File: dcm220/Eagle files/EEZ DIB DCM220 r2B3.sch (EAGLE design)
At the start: 228 parts, among them IC1 Si8662AB-B-IS1, IC10 LT3763EFE#PBF, IC11 MC33274ADR2G, IC12 LT3763EFE#PBF, IC2 TPS54060DGQ, IC3 Si8641AB-B-IS1, IC4 M24C32-WMN6P, IC5 LP2985-33DBVR, IC6 TPD4E001DRLR, IC7 MAX5715BAUD+, IC8 STM32F373C8T6, IC9 MC33272ADR2G, J1 4907, J2 571-0500, J3 571-0100, J4 571-0500, J5 571-0100, Q1 IRFR7546TRPBF, Q2 IRFR7546TRPBF, Q3 2N7002, Q4 BSS84, Q5 IRFR7546TRPBF, Q6 IRFR7546TRPBF, Q7 2N7002, Q8 BSS84, X1 172648-0102, X2 77317-104-28LF, X3 22-23-2061, X4 DS1024-2*5R0, Y1 LF XTAL026392

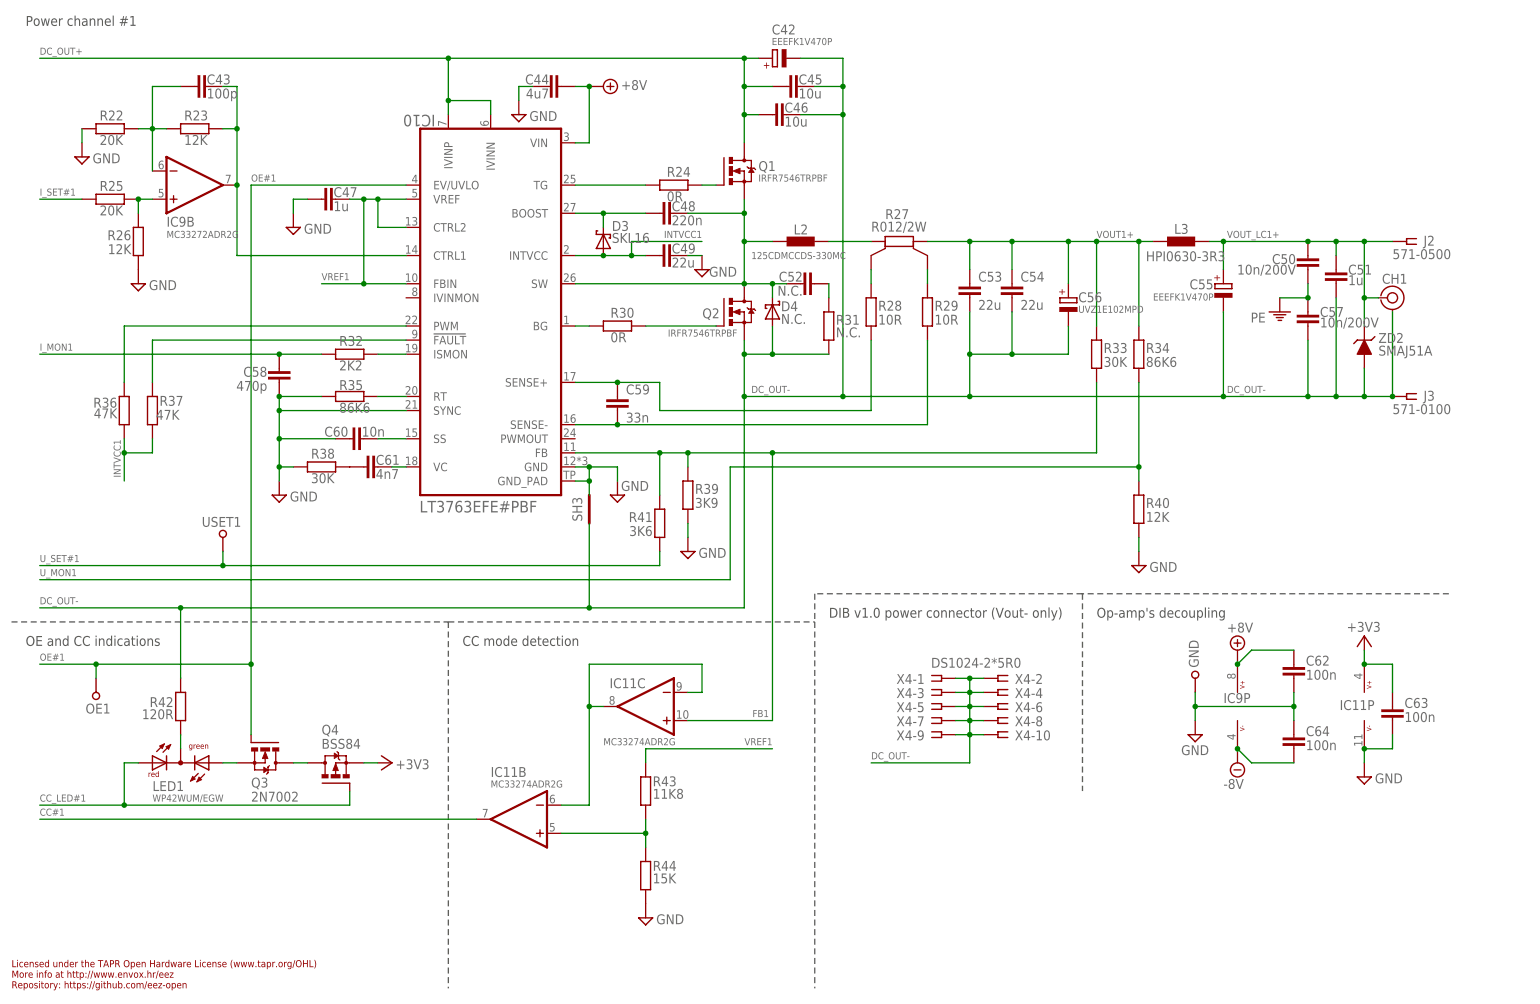
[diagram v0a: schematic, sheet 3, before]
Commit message: #48, replaced DAC with PWM
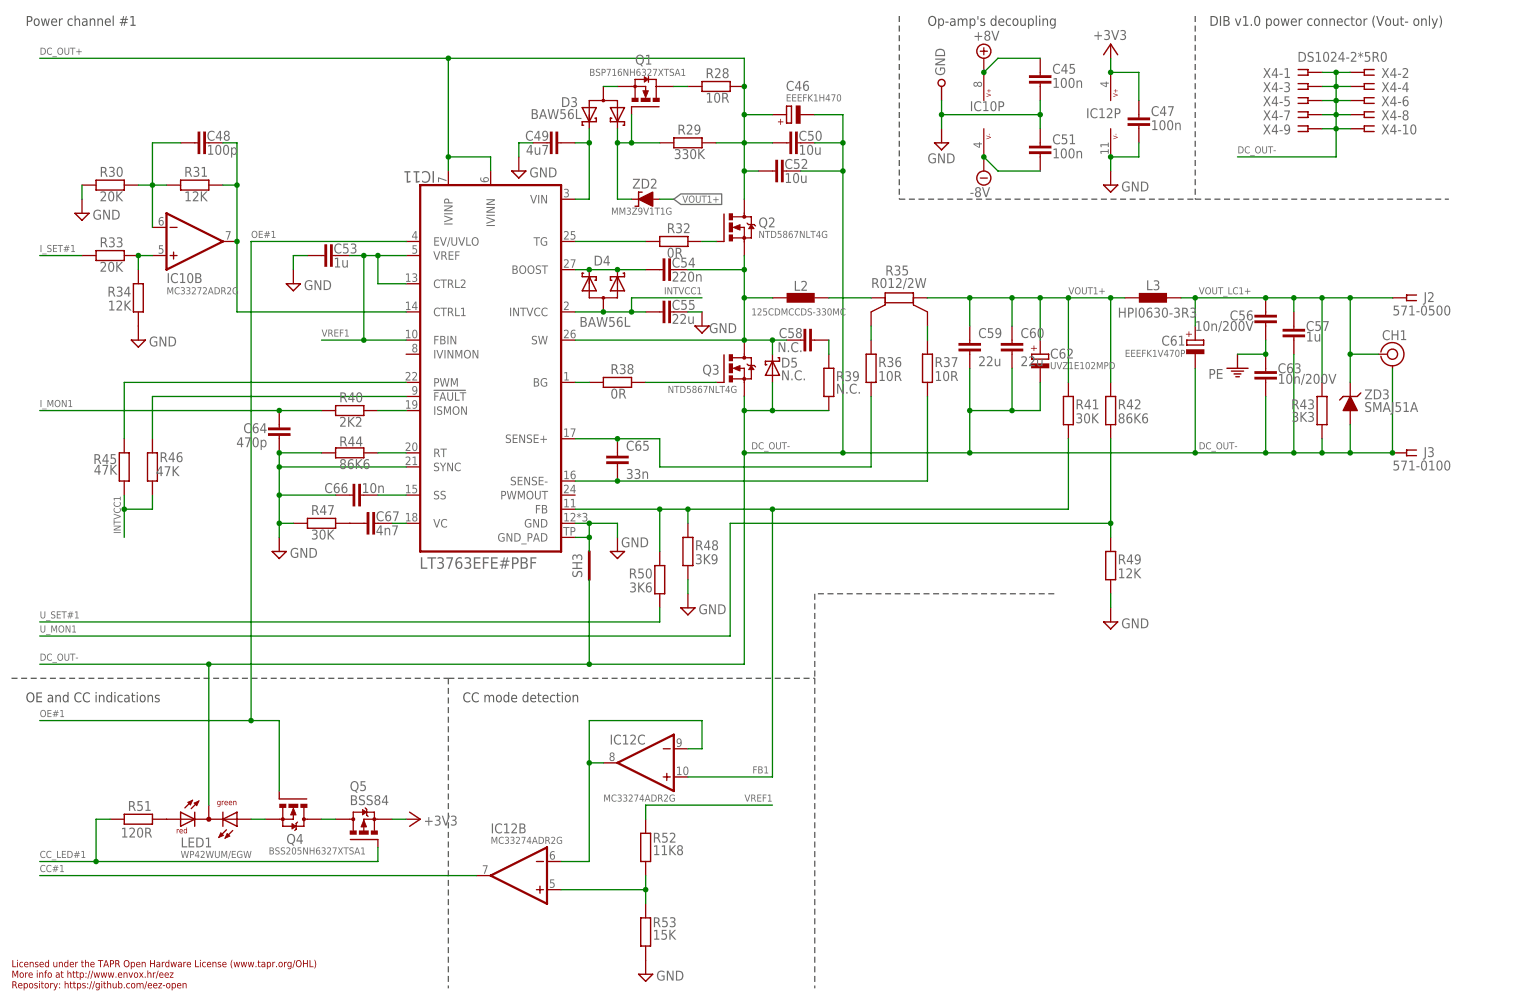
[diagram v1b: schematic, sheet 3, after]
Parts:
- removed ISET1, OE1, USET1: (no value), EEZ_connectors:TEST-PIN_0.9MM
- removed JP4: JP2-CUT, EEZ_Lib1:JP2-CUT
- removed JP5: JP2-NOCUT, EEZ_Lib1:JP2-NOCUT
- added C85: 33n, rcl:C-EUC0805
- added C86: 10n, rcl:C-EUC0805
- added C87: 4n7, rcl:C-EUC0805
- added D7: BAW56L, EEZ_Lib1:BAW56L
- added D8: N.C., EEZ_Lib1:SCHOTTKYSMA_DO-214AC
- added IC13: LT3763EFE#PBF, EEZ_Lib1:LT3763EFE#PBF
- added Q10: BSS84, EEZ_Lib1:IRLML2246TRPBF
- added Q9: BSS205NH6327XTSA1, EEZ_Lib1:2N7002
- added R68, R70: 86K6, rcl:R-EU_R0805
- added R69: 3K3, rcl:R-EU_R0805
- added R71, R72: 47K, rcl:R-EU_R0805
- added R73: 30K, rcl:R-EU_R0805
- added R74: 3K9, rcl:R-EU_R0805
- added R75: 12K, rcl:R-EU_R0805
- added R76: 3K6, rcl:R-EU_R0805
- added R77: 120R, rcl:R-EU_R0805
- added R78: 11K8, rcl:R-EU_R0805
- added R79: 15K, rcl:R-EU_R0805
- added ZD4: MM3Z9V1T1G, EEZ_Lib1:ZENER-DIODESOD323
- added ZD5: SMAJ51A, EEZ_Lib1:P6SMB68A
- C1, C2, C3: value 4n7/100V -> 10n/200V
- C15: value 100n -> 10n; device rcl:C-EUC0603 -> rcl:C-EUC0805
- C25: value 100n -> N.C.
- C26, C27: value 4u7 -> 100n; device rcl:C-EUC1206 -> rcl:C-EUC0603
- C29: value 100n -> 4u7; device rcl:C-EUC0603 -> rcl:C-EUC1206
- C30, C31: value 18p -> 100n
- C32: value 100n -> 4p7
- C33: value 10n -> 4p7; device rcl:C-EUC0805 -> rcl:C-EUC0603
- C35: value 1u -> 10n
- C36: value 100p -> 1n
- C38: value 3n3 -> 1u
- C39, C41: value 3n3 -> 4n7
- C40: value 3n3 -> 100n; device rcl:C-EUC0805 -> rcl:C-EUC0603
- C42: value EEEFK1V470P -> 4n7; device EEZ_Lib1:ECAPSMD8.3MM/HA0 -> rcl:C-EUC0805
- C43: value 100p -> 4n7
- C44, C67: value 4u7 -> 4n7; device rcl:C-EUC1206 -> rcl:C-EUC0805
- C45: value 10u -> 100n; device rcl:C-EUC1210 -> rcl:C-EUC0603
- C46, C68: value 10u -> EEEFK1H470; device rcl:C-EUC1210 -> EEZ_Lib1:ECAPSMD8.3MM/HA0
- C47, C51: value 1u -> 100n; device rcl:C-EUC0805 -> rcl:C-EUC0603
- C48: value 220n -> 100p
- C49: value 22u -> 4u7; device rcl:C-EUC1210 -> rcl:C-EUC1206
- C50: value 10n/200V -> 10u; device rcl:C-EUC1206 -> rcl:C-EUC1210
- C52: value N.C. -> 10u; device rcl:C-EUC0805 -> rcl:C-EUC1210
- C53, C77: value 22u -> 1u; device rcl:C-EUC1210 -> rcl:C-EUC0805
- C54: value 22u -> 220n; device rcl:C-EUC1210 -> rcl:C-EUC0805
- C55: value EEEFK1V470P -> 22u; device EEZ_Lib1:ECAPSMD8.3MM/HA0 -> rcl:C-EUC1210
- C56: value UVZ1E102MPD -> 10n/200V; device EEZ_Lib1:ECAP5G_10.5MM -> rcl:C-EUC1206
- C57, C73: value 10n/200V -> 1u; device rcl:C-EUC1206 -> rcl:C-EUC0805
- C58: value 470p -> N.C.
- C59: value 33n -> 22u; device rcl:C-EUC0805 -> rcl:C-EUC1210
- C60: value 10n -> 22u; device rcl:C-EUC0805 -> rcl:C-EUC1210
- C61: value 4n7 -> EEEFK1V470P; device rcl:C-EUC0805 -> EEZ_Lib1:ECAPPANASONIC_H
- C62: value 100n -> UVZ1E102MPD; device rcl:C-EUC0603 -> EEZ_Lib1:ECAP5G_10.5MM
- C63: value 100n -> 10n/200V; device rcl:C-EUC0603 -> rcl:C-EUC1206
- C64: value 100n -> 470p; device rcl:C-EUC0603 -> rcl:C-EUC0805
- C65: value EEEFK1V470P -> 33n; device EEZ_Lib1:ECAPSMD8.3MM/HA0 -> rcl:C-EUC0805
- C66: value 100p -> 10n
- C69: value 10u -> 100p; device rcl:C-EUC1210 -> rcl:C-EUC0805
- C70: value 1u -> 4u7; device rcl:C-EUC0805 -> rcl:C-EUC1206
- C71: value 220n -> 10u; device rcl:C-EUC0805 -> rcl:C-EUC1210
- C72: value 22u -> 10u
- C74: value 1u -> 220n
- C75: value N.C. -> 22u; device rcl:C-EUC0805 -> rcl:C-EUC1210
- C76: value 22u -> 10n/200V; device rcl:C-EUC1210 -> rcl:C-EUC1206
- C78: value EEEFK1V470P -> N.C.; device EEZ_Lib1:ECAPSMD8.3MM/HA0 -> rcl:C-EUC0805
- C79: value UVZ1E102MPD -> 22u; device EEZ_Lib1:ECAP5G_10.5MM -> rcl:C-EUC1210
- C80: value 10n/200V -> 22u; device rcl:C-EUC1206 -> rcl:C-EUC1210
- C81: value 470p -> EEEFK1V470P; device rcl:C-EUC0805 -> EEZ_Lib1:ECAPPANASONIC_H
- C82: value 33n -> UVZ1E102MPD; device rcl:C-EUC0805 -> EEZ_Lib1:ECAP5G_10.5MM
- C83: value 10n -> 10n/200V; device rcl:C-EUC0805 -> rcl:C-EUC1206
- C84: value 4n7 -> 470p
- D3: value SKL16 -> BAW56L; device EEZ_Lib1:SCHOTTKYSOD123 -> EEZ_Lib1:BAW56L
- D4, D6: value N.C. -> BAW56L; device EEZ_Lib1:SCHOTTKYSMA_DO-214AC -> EEZ_Lib1:BAW56L
- D5: value SKL16 -> N.C.; device EEZ_Lib1:SCHOTTKYSOD123 -> EEZ_Lib1:SCHOTTKYSMA_DO-214AC
- IC10: value LT3763EFE#PBF -> MC33272ADR2G; device EEZ_Lib1:LT3763EFE#PBF -> EEZ_Lib1:TL072SOIC8
- IC11: value MC33274ADR2G -> LT3763EFE#PBF; device EEZ_Lib1:TL074SOIC14 -> EEZ_Lib1:LT3763EFE#PBF
- IC12: value LT3763EFE#PBF -> MC33274ADR2G; device EEZ_Lib1:LT3763EFE#PBF -> EEZ_Lib1:TL074SOIC14
- IC6: value TPD4E001DRLR -> 74HC2G04GW,125; device EEZ_Lib1:TPD4E001-DRL -> EEZ_Lib1:74HC2G04
- IC7: value MAX5715BAUD+ -> N.C.; device EEZ_Lib1:MAX5715BAUD+ -> EEZ_Lib1:TPD4E001-DRL
- IC9: value MC33272ADR2G -> TL431B; device EEZ_Lib1:TL072SOIC8 -> EEZ_Lib1:TL431
- JP2: value JP2-NOCUT -> JP2-CUT; device EEZ_Lib1:JP2-NOCUT -> EEZ_Lib1:JP2-CUT
- Q1, Q6: value IRFR7546TRPBF -> BSP716NH6327XTSA1; device EEZ_Lib1:N-MOSFETDPAK -> transistor-power:N-HEXFET-2D_SOT232-IRLL014N
- Q2: value IRFR7546TRPBF -> NTD5867NLT4G
- Q3, Q7: value 2N7002 -> NTD5867NLT4G; device EEZ_Lib1:2N7002 -> EEZ_Lib1:N-MOSFETDPAK
- Q4: value BSS84 -> BSS205NH6327XTSA1; device EEZ_Lib1:IRLML2246TRPBF -> EEZ_Lib1:2N7002
- Q5: value IRFR7546TRPBF -> BSS84; device EEZ_Lib1:N-MOSFETDPAK -> EEZ_Lib1:IRLML2246TRPBF
- Q8: value BSS84 -> NTD5867NLT4G; device EEZ_Lib1:IRLML2246TRPBF -> EEZ_Lib1:N-MOSFETDPAK
- R1: value 4K7/2W -> N.C.
- R16, R17: value 3K3 -> 10K
- R18, R20: value 1K -> 10K
- R19: value 1K -> N.C.
- R21: value 1K -> 3K3
- R22: value 20K -> 3K3
- R23: value 12K -> 120R
- R24: value 0R -> 2K2
- R25: value 20K -> 2K2
- R26, R40: value 12K -> 2K2
- R27: value R012/2W -> 2K2; device EEZ_Lib1:R-EU_4WIRE2512 -> rcl:R-EU_R0805
- R29: value 10R -> 330K
- R30: value 0R -> 20K
- R31: value N.C. -> 12K; device rcl:R-EU_R1206 -> rcl:R-EU_R0805
- R32: value 2K2 -> 0R
- R33, R56: value 30K -> 20K
- R34, R57: value 86K6 -> 12K
- R35: value 86K6 -> R012/2W; device rcl:R-EU_R0805 -> EEZ_Lib1:R-EU_4WIRE2512
- R36, R37: value 47K -> 10R
- R38: value 30K -> 0R
- R39: value 3K9 -> N.C.; device rcl:R-EU_R0805 -> rcl:R-EU_R1206
- R41: value 3K6 -> 30K
- R42: value 120R -> 86K6
- R43: value 11K8 -> 3K3
- R44: value 15K -> 86K6
- R45: value 20K -> 47K
- R46: value 12K -> 47K
- R47: value 0R -> 30K
- R48: value 20K -> 3K9
- R50: value R012/2W -> 3K6; device EEZ_Lib1:R-EU_4WIRE2512 -> rcl:R-EU_R0805
- R51: value 10R -> 120R
- R52: value 10R -> 11K8
- R53: value 0R -> 15K
- R54: value N.C. -> 10R; device rcl:R-EU_R1206 -> rcl:R-EU_R0805
- R55: value 2K2 -> 330K
- R58: value 86K6 -> 0R
- R59: value 47K -> 20K
- R60: value 47K -> 12K
- R61: value 30K -> R012/2W; device rcl:R-EU_R0805 -> EEZ_Lib1:R-EU_4WIRE2512
- R62: value 3K9 -> 10R
- R63: value 12K -> 10R
- R64: value 3K6 -> 0R
- R65: value 120R -> N.C.; device rcl:R-EU_R0805 -> rcl:R-EU_R1206
- R66: value 11K8 -> 2K2
- R67: value 15K -> 30K
- RN2: value DR1206-33R-4/8 -> N.C.
- X3: value 22-23-2061 -> N.C.
- ZD2: value SMAJ51A -> MM3Z9V1T1G; device EEZ_Lib1:P6SMB68A -> EEZ_Lib1:ZENER-DIODESOD323
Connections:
- removed net !DAC_CLR: IC7.!CLR, JP3.1
- removed net !LDAC: IC7.!LDAC, JP2.1
- removed net DAC_MOSI: IC7.DIN, IC8.PF6
- removed net DAC_NSS: IC7.CSB, IC8.PA4
- removed net DAC_SCLK: IC7.SCLK, IC8.PA5
- removed net N$266: IC7.OUTB, ISET1.P$1, I_SET1.2
- removed net N$277: C66.1, IC12.CTRL1, IC9A.OUT, R46.2
- removed net N$35: LED2.C, R65.1
- removed net N$477: IC7.OUTC, I_SET2.2
- removed net N$479: IC7.OUTD, U_SET2.2
- removed net N$52: C36.2, IC8.VREFSD+, JP5.1
- removed net REF_12: IC7.REF, JP5.2
- new net +VREF: C39.2, IC8.VREFSD+, IC9.C, IC9.R, R23.2
- new net ISET1: C48.1, IC10B.OUT, IC11.CTRL1, R31.2
- new net ISET2: C69.1, IC10A.OUT, IC13.CTRL1, R57.2
- new net I_SET_OUT#1: IC6A.I, IC8.PB8, R14.2
- new net I_SET_OUT#2: IC6B.I, IC8.PB9, R17.2
- new net N$246: C24.2, R16.1
- new net N$247: C24.1, C26.1, I_SET1.2, R14.1
- new net N$25: LED2.AR, R77.1
- new net N$26: D3.K1, Q1.G, R29.2, ZD2.C
- new net N$39: C49.1, D3.K2, IC11.VIN
- new net N$40: C30.2, R18.1
- new net N$42: C70.1, D6.K2, IC13.VIN
- new net N$43: D3.CA, Q1.S
- new net N$44: C30.1, C31.1, I_SET2.2, R17.1
- new net N$46: D6.K1, Q6.G, R55.2, ZD4.C
- new net N$61: D6.CA, Q6.S
- new net NRST: C36.1, IC8.NRST, JP3.2, R20.2, RN2-3.1
- new net Q1D: Q1.D, R28.2
- new net Q6D: Q6.D, R54.2
- new net U_SET_OUT#1: IC8.PA6, U_SET1.2
- new net U_SET_OUT#2: IC8.PA5, U_SET2.2
- net !RESET: now also JP3.1; no longer IC8.NRST, JP3.2, RN2-4.1
- net +3V3: now also C25.1, C29.1, C36.2, C40.2, C47.1, IC12P.V+, IC6P.V+, IC7.VCC, JP2.1, Q10.S, Q5.S, R20.1, R23.1; no longer C24.1, C25.2, C26.1, C29.2, C37.2, C63.1, IC11P.V+, IC6.VCC, IC7.VDD, IC7.VDDIO, JP4.1, Q4.S, Q8.S
- net +8V: now also C45.1, IC10P.V+; no longer C44.1, C62.1, C67.1, IC10.VIN, IC12.VIN, IC9P.V+
- net -8V: now also C51.2, IC10P.V-; no longer C64.2, IC9P.V-
- net AGND: now also C39.1; no longer C36.1
- net BOOT0: now also R15.2; no longer R14.2
- net CC#1: now also IC12B.OUT; no longer IC11B.OUT
- net CC#2: now also IC12A.OUT; no longer IC11A.OUT
- net CC_LED#1: now also Q5.G, R51.2; no longer LED1.AR, Q4.G
- net CC_LED#2: now also Q10.G, R77.2; no longer LED2.AR, Q8.G
- net DC_OUT+: now also C46.+, C50.1, C52.1, C68.+, C71.1, C72.1, IC11.IVINN, IC11.IVINP, IC13.IVINN, IC13.IVINP, Q2.D, Q7.D, R28.1, R29.1, R54.1, R55.1; no longer C42.+, C45.1, C46.1, C65.+, C68.1, C69.1, IC10.IVINN, IC10.IVINP, IC12.IVINN, IC12.IVINP, Q1.D, Q5.D
- net DC_OUT-: now also C46.-, C50.2, C52.2, C59.2, C60.2, C61.-, C62.-, C63.2, C68.-, C71.2, C72.2, C79.2, C81.-, C82.-, C83.2, D5.A, D8.A, LED1.C, LED2.C, Q3.S, Q8.S, R39.1, R43.2, R65.1, R69.2, ZD5.A; no longer C42.-, C45.2, C46.2, C51.2, C53.2, C54.2, C55.-, C56.-, C65.-, C68.2, C69.2, C74.2, C76.2, C78.-, C79.-, D4.A, D6.A, Q2.S, Q6.S, R31.1, R42.2, R54.1, R65.2, ZD2.A
- net FB1: now also IC11.FB, IC12C.+IN, R41.1, R48.2, R50.2; no longer IC10.FB, IC11C.+IN, R33.1, R39.2, R41.2
- net FB2: now also IC12D.+IN, IC13.FB, R67.1, R74.2, R76.2; no longer IC11D.+IN, IC12.FB, R56.1, R62.2, R64.2
- net GND: now also C25.2, C29.2, C31.2, C42.1, C43.1, C44.1, C45.2, C51.1, C53.2, C55.2, C66.1, C73.2, C75.2, C84.1, C86.1, IC11.GND, IC11.GND_PAD, IC11.SYNC, IC12P.V-, IC13.GND, IC13.GND_PAD, IC13.SYNC, IC6P.V-, IC9.A, R19.1, R21.2, R22.2, R30.1, R34.1, R47.1, R48.1, R53.1, R56.1, R60.1, R70.1, R73.1, R74.1, R75.1, R79.1; no longer C24.2, C25.1, C29.1, C30.1, C31.1, C39.1, C44.2, C58.1, C60.1, C62.2, C63.2, C67.2, C72.2, C81.1, C83.1, IC10.GND, IC10.GND_PAD, IC10.SYNC, IC11P.V-, IC12.GND, IC12.GND_PAD, IC12.SYNC, IC6.GND, JP2.2, R14.1, R16.2, R17.2, R22.1, R26.1, R35.1, R38.1, R39.1, R40.1, R45.1, R58.1, R61.1, R62.1, R63.1, R67.1
- net INTVCC1: now also C55.1, D4.CA, IC11.INTVCC, R45.1, R46.2; no longer C49.1, D3.A, IC10.INTVCC, R36.1, R37.2
- net INTVCC2: now also C75.1, D7.CA, IC13.INTVCC, R71.1, R72.2; no longer C72.1, D5.A, IC12.INTVCC, R59.1, R60.2
- net I_MON#1: now also C42.2, R25.1; no longer C39.2, R19.1
- net I_MON#2: now also C44.2, R27.1; no longer C41.2, R21.1
- net I_MON1: now also C64.2, R25.2, R40.1; no longer C58.2, R19.2, R32.1
- net I_MON2: now also C84.2, R27.2, R66.1; no longer C81.2, R21.2, R55.1
- net I_SET#1: now also R33.1; no longer R25.1
- net I_SET#2: now also R59.1; no longer R48.1
- net LOUT1: now also R35.1; no longer R27.1
- net LOUT2: now also R61.1; no longer R50.1
- net N$1: now also IC11.BG, R38.1; no longer IC10.BG, R30.1
- net N$11: now also LED1.AR, R51.1; no longer LED1.C, R42.1
- net N$12: now also C66.2, IC11.SS; no longer C60.2, IC10.SS
- net N$13: now also C67.1, R47.2; no longer C61.1, R38.2
- net N$14: now also C67.2, IC11.VC; no longer C61.2, IC10.VC
- net N$15: now also IC11.TG, R32.1; no longer IC10.TG, R24.1
- net N$16: now also R35.2S, R37.2; no longer R27.2S, R29.2
- net N$17: now also C58.2, R39.2; no longer C52.2, R31.2
- net N$18: now also IC11.!FAULT, R46.1; no longer IC10.!FAULT, R37.1
- net N$19: now also Q2.G, R32.2; no longer Q1.G, R24.2
- net N$2: now also Q3.G, R38.2; no longer Q2.G, R30.2
- net N$22: now also C54.1, D4.K1, D4.K2, IC11.BOOST; no longer C48.1, D3.C, IC10.BOOST
- net N$249: now also C87.2, IC13.VC; no longer C84.2, IC12.VC
- net N$250: now also IC10B.+IN, R33.2, R34.2; no longer IC9B.+IN, R25.2, R26.2
- net N$251: now also C48.2, IC10B.-IN, R30.2, R31.1; no longer C43.2, IC9B.-IN, R22.2, R23.1
- net N$252: now also IC6A.O, R16.2; no longer C43.1, IC10.CTRL1, IC9B.OUT, R23.2
- net N$253: now also IC13.!FAULT, R72.1; no longer IC12.!FAULT, R60.1
- net N$255: now also IC13.TG, R58.1; no longer IC12.TG, R47.1
- net N$256: now also Q7.G, R58.2; no longer Q5.G, R47.2
- net N$257: now also IC13.BG, R64.1; no longer IC12.BG, R53.1
- net N$258: now also Q8.G, R64.2; no longer Q6.G, R53.2
- net N$261: now also R61.1S, R62.2; no longer R50.1S, R51.2
- net N$262: now also R61.2S, R63.2; no longer R50.2S, R52.2
- net N$263: now also C78.2, R65.2; no longer C75.2, R54.2
- net N$264: now also C74.1, D7.K1, D7.K2, IC13.BOOST; no longer C71.1, D5.C, IC12.BOOST
- net N$267: now also IC13.ISMON, R66.2; no longer IC12.ISMON, R55.2
- net N$27: now also Q4.S; no longer Q3.S
- net N$270: now also IC12A.-IN, IC12D.-IN, IC12D.OUT; no longer IC11A.-IN, IC11D.-IN, IC11D.OUT
- net N$271: now also IC12A.+IN, R78.1, R79.2; no longer IC11A.+IN, R66.1, R67.2
- net N$278: now also C69.2, IC10A.-IN, R56.2, R57.1; no longer C66.2, IC9A.-IN, R45.2, R46.1
- net N$28: now also IC13.RT, R70.2; no longer IC12.RT, R58.2
- net N$3: now also Q5.D; no longer Q3.D
- net N$311: now also IC10A.+IN, R59.2, R60.2; no longer IC9A.+IN, R48.2, R49.2
- net N$36: now also C86.2, IC13.SS; no longer C83.2, IC12.SS
- net N$37: now also C87.1, R73.2; no longer C84.1, R61.2
- net N$38: now also Q10.D, Q9.D; no longer Q7.D, Q8.D
- net N$41: now also Q9.S; no longer Q7.S
- net N$45: now also IC6B.O, R18.2; no longer IC7.OUTA, U_SET1.2
- net N$48: now also IC11.ISMON, R40.2; no longer IC10.ISMON, R32.2
- net N$49: now also IC7.IO1; no longer IC6.IO1
- net N$50: now also IC7.IO2, RN2-3.2; no longer IC6.IO2, RN2-4.2
- net N$51: now also JP2.2, R19.2; no longer JP4.2, R15.2
- net N$54: now also IC12B.+IN, R52.1, R53.2; no longer IC11B.+IN, R43.1, R44.2
- net N$55: now also IC12B.-IN, IC12C.-IN, IC12C.OUT; no longer IC11B.-IN, IC11C.-IN, IC11C.OUT
- net N$7: now also R35.1S, R36.2; no longer R27.1S, R28.2
- net N$8: now also IC11.RT, R44.2; no longer IC10.RT, R35.2
- net OE#1: now also IC11.EV/UVLO, Q4.G; no longer IC10.EV/UVLO, OE1.P$1, Q3.G
- net OE#2: now also IC13.EV/UVLO, Q9.G; no longer IC12.EV/UVLO, Q7.G
- net PE: now also C56.1, C63.1, C76.1, C83.1; no longer C50.1, C57.1, C73.1, C80.1
- net PWM#1: now also IC11.PWM, R45.2; no longer IC10.PWM, R36.2
- net PWM#2: now also IC13.PWM, R71.2; no longer IC12.PWM, R59.2
- net RCC_OSC_IN: now also C32.2; no longer C30.2
- net RCC_OSC_OUT: now also C33.2; no longer C31.2
- net SENSE1+: now also C65.1, IC11.SENSE+, R36.1; no longer C59.1, IC10.SENSE+, R28.1
- net SENSE1+1: now also C85.1, IC13.SENSE+, R62.1; no longer C82.1, IC12.SENSE+, R51.1
- net SENSE1-: now also C65.2, IC11.SENSE-, R37.1; no longer C59.2, IC10.SENSE-, R29.1
- net SENSE1-1: now also C85.2, IC13.SENSE-, R63.1; no longer C82.2, IC12.SENSE-, R52.1
- net SW1: now also C54.2, C58.1, D5.C, IC11.SW, Q2.S, Q3.D; no longer C48.2, C52.1, D4.C, IC10.SW, Q1.S, Q2.D
- net SW2: now also C74.2, C78.1, D8.C, IC13.SW, Q7.S, Q8.D; no longer C71.2, C75.1, D6.C, IC12.SW, Q5.S, Q6.D
- net SWDIO: now also RN2-4.1; no longer RN2-3.1
- net TCK: now also IC7.IO4; no longer IC6.IO4
- net TEMP#1: now also C34.2, R21.1; no longer C33.2, R16.1
- net TEMP#2: now also C35.2, IC8.PA4, R22.1; no longer C34.2, IC8.PA6, R17.1
- net TMS: now also IC7.IO3, RN2-4.2; no longer IC6.IO3, RN2-3.2
- net U_MON#1: now also C41.2, R24.1; no longer C38.2, R18.1
- net U_MON#2: now also C43.2, R26.1; no longer C40.2, R20.1
- net U_MON1: now also R24.2, R42.1, R49.2; no longer R18.2, R34.1, R40.2
- net U_MON2: now also R26.2, R68.1, R75.2; no longer R20.2, R57.1, R63.2
- net U_SET#1: now also R50.1; no longer R41.1, USET1.P$1
- net U_SET#2: now also R76.1; no longer R64.1
- net VDDA: now also C37.2, C38.2; no longer C32.2, C35.2
- net VOUT1+: now also C59.1, C60.1, C62.+, R35.2, R41.2, R42.2, ZD2.A; no longer C53.1, C54.1, C56.+, R27.2, R33.2, R34.2
- net VOUT2+: now also C79.1, C80.1, C82.+, R61.2, R67.2, R68.2, ZD4.A; no longer C76.1, C77.1, C79.+, R50.2, R56.2, R57.2
- net VOUT_LC1+: now also C56.2, C57.1, C61.+, R43.1, ZD3.C; no longer C50.2, C51.1, C55.+, ZD2.C
- net VOUT_LC2+: now also C76.2, C77.1, C81.+, R69.1, ZD5.C; no longer C73.2, C74.1, C78.+, ZD3.C
- net VREF1: now also C53.1, IC11.CTRL2, IC11.FBIN, IC11.VREF, R52.2; no longer C47.1, IC10.CTRL2, IC10.FBIN, IC10.VREF, R43.2
- net VREF2: now also C73.1, IC13.CTRL2, IC13.FBIN, IC13.VREF, R78.2; no longer C70.1, IC12.CTRL2, IC12.FBIN, IC12.VREF, R66.2
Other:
- note added: "Optional JTAG (SWD)"
- note added: "Voltage reference"
- note removed: "4-ch DAC"
- note removed: "JTAG (SWD)"
- moved on the sheet: C24, C25, C26, C27, C28, C29, C30, C31, C32, C33, C34, C35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

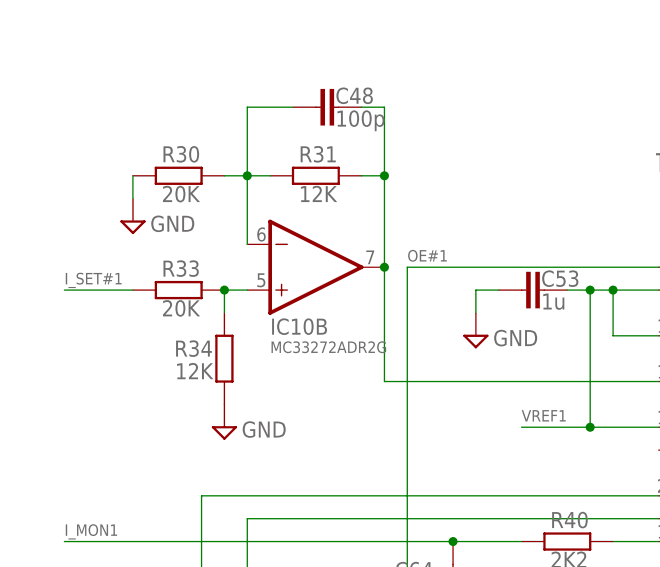
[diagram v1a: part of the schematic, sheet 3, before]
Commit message: DCM220 I_SET gain adjustment
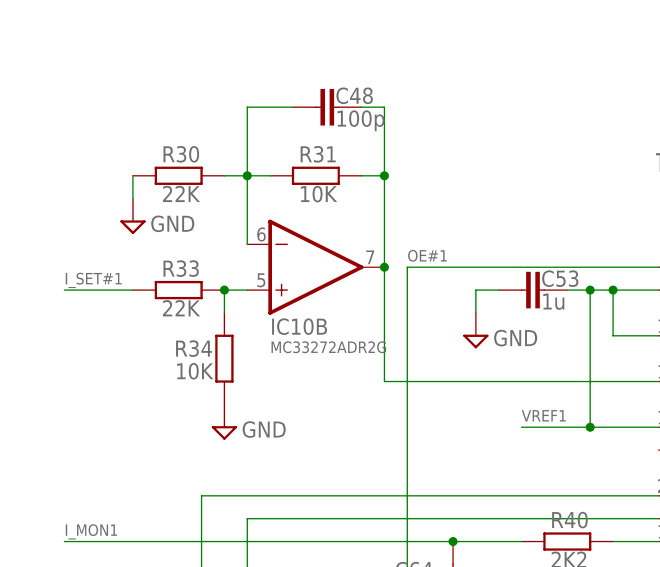
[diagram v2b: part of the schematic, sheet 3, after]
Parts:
- R30, R33, R56, R59: value 20K -> 22K
- R31, R34, R57, R60: value 12K -> 10K
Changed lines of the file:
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@@
 <setting verticaltext="up"/>
 </settings>
-<grid distance="0.025" unitdist="inch" unit="inch" style="lines" multiple="4" display="no" altdistance="0.01" altunitdist="inch" altunit="inch"/>
+<grid distance="0.1" unitdist="inch" unit="inch" style="lines" multiple="1" display="no" altdistance="0.01" altunitdist="inch" altunit="inch"/>
 <layers>
 <layer number="1" name="Top" color="4" fill="1" visible="no" active="no"/>
@@
 <part name="Q4" library="EEZ_Lib1" deviceset="2N7002" device="" value="BSS205NH6327XTSA1"/>
 <part name="IC10" library="EEZ_Lib1" deviceset="TL072" device="SOIC8" value="MC33272ADR2G"/>
-<part name="R31" library="rcl" deviceset="R-EU_" device="R0805" value="12K"/>
-<part name="R30" library="rcl" deviceset="R-EU_" device="R0805" value="20K"/>
+<part name="R31" library="rcl" deviceset="R-EU_" device="R0805" value="10K"/>
+<part name="R30" library="rcl" deviceset="R-EU_" device="R0805" value="22K"/>
 <part name="SUPPLY20" library="supply2" deviceset="GND" device=""/>
 <part name="C45" library="rcl" deviceset="C-EU" device="C0603" value="100n"/>
@@
 <part name="C80" library="rcl" deviceset="C-EU" device="C1210" value="22u"/>
 <part name="Q9" library="EEZ_Lib1" deviceset="2N7002" device="" value="BSS205NH6327XTSA1"/>
-<part name="R57" library="rcl" deviceset="R-EU_" device="R0805" value="12K"/>
-<part name="R56" library="rcl" deviceset="R-EU_" device="R0805" value="20K"/>
+<part name="R57" library="rcl" deviceset="R-EU_" device="R0805" value="10K"/>
+<part name="R56" library="rcl" deviceset="R-EU_" device="R0805" value="22K"/>
 <part name="SUPPLY30" library="supply2" deviceset="GND" device=""/>
 <part name="C75" library="rcl" deviceset="C-EU" device="C1210" value="22u"/>
@@
 <part name="PE3" library="supply1" deviceset="PE" device=""/>
 <part name="L4" library="EEZ_inductors_and_transformers" deviceset="125CDMCC/DS" device="" value="125CDMCCDS-330MC"/>
-<part name="R34" library="rcl" deviceset="R-EU_" device="R0805" value="12K"/>
-<part name="R33" library="rcl" deviceset="R-EU_" device="R0805" value="20K"/>
+<part name="R34" library="rcl" deviceset="R-EU_" device="R0805" value="10K"/>
+<part name="R33" library="rcl" deviceset="R-EU_" device="R0805" value="22K"/>
 <part name="SUPPLY18" library="supply2" deviceset="GND" device=""/>
-<part name="R60" library="rcl" deviceset="R-EU_" device="R0805" value="12K"/>
-<part name="R59" library="rcl" deviceset="R-EU_" device="R0805" value="20K"/>
+<part name="R60" library="rcl" deviceset="R-EU_" device="R0805" value="10K"/>
+<part name="R59" library="rcl" deviceset="R-EU_" device="R0805" value="22K"/>
 <part name="SUPPLY19" library="supply2" deviceset="GND" device=""/>
 <part name="GND" library="EEZ_connectors" deviceset="TEST-PIN" device="_0.9MM"/>
